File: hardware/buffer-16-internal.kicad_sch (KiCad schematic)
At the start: 6 parts, among them U2 SN74LVC8T245DWRG4, U3 SN74LVC8T245DWRG4

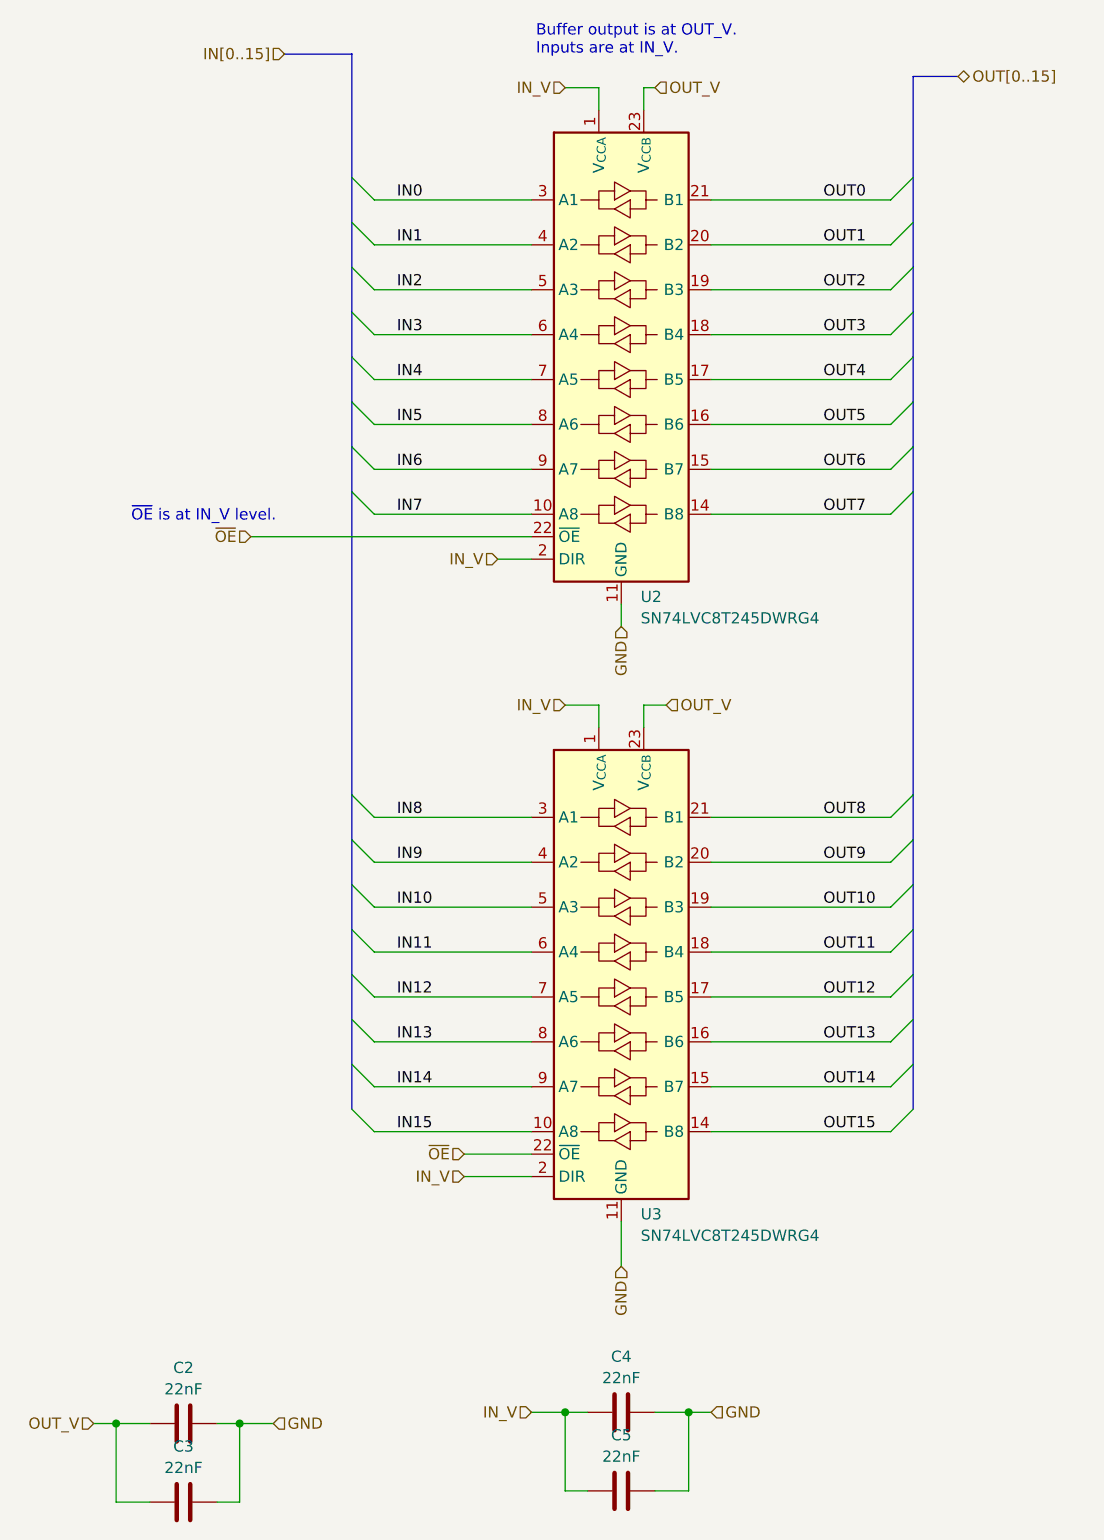
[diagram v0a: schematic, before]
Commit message: Massively reorganize board designs
Now planning to have most assembly done by JLCPCB, so trace sizes,
part selections, etc. are set accordingly.

New boards are:
 - cartridge interface & flash
 - microcontroller & registers
 - sram x2
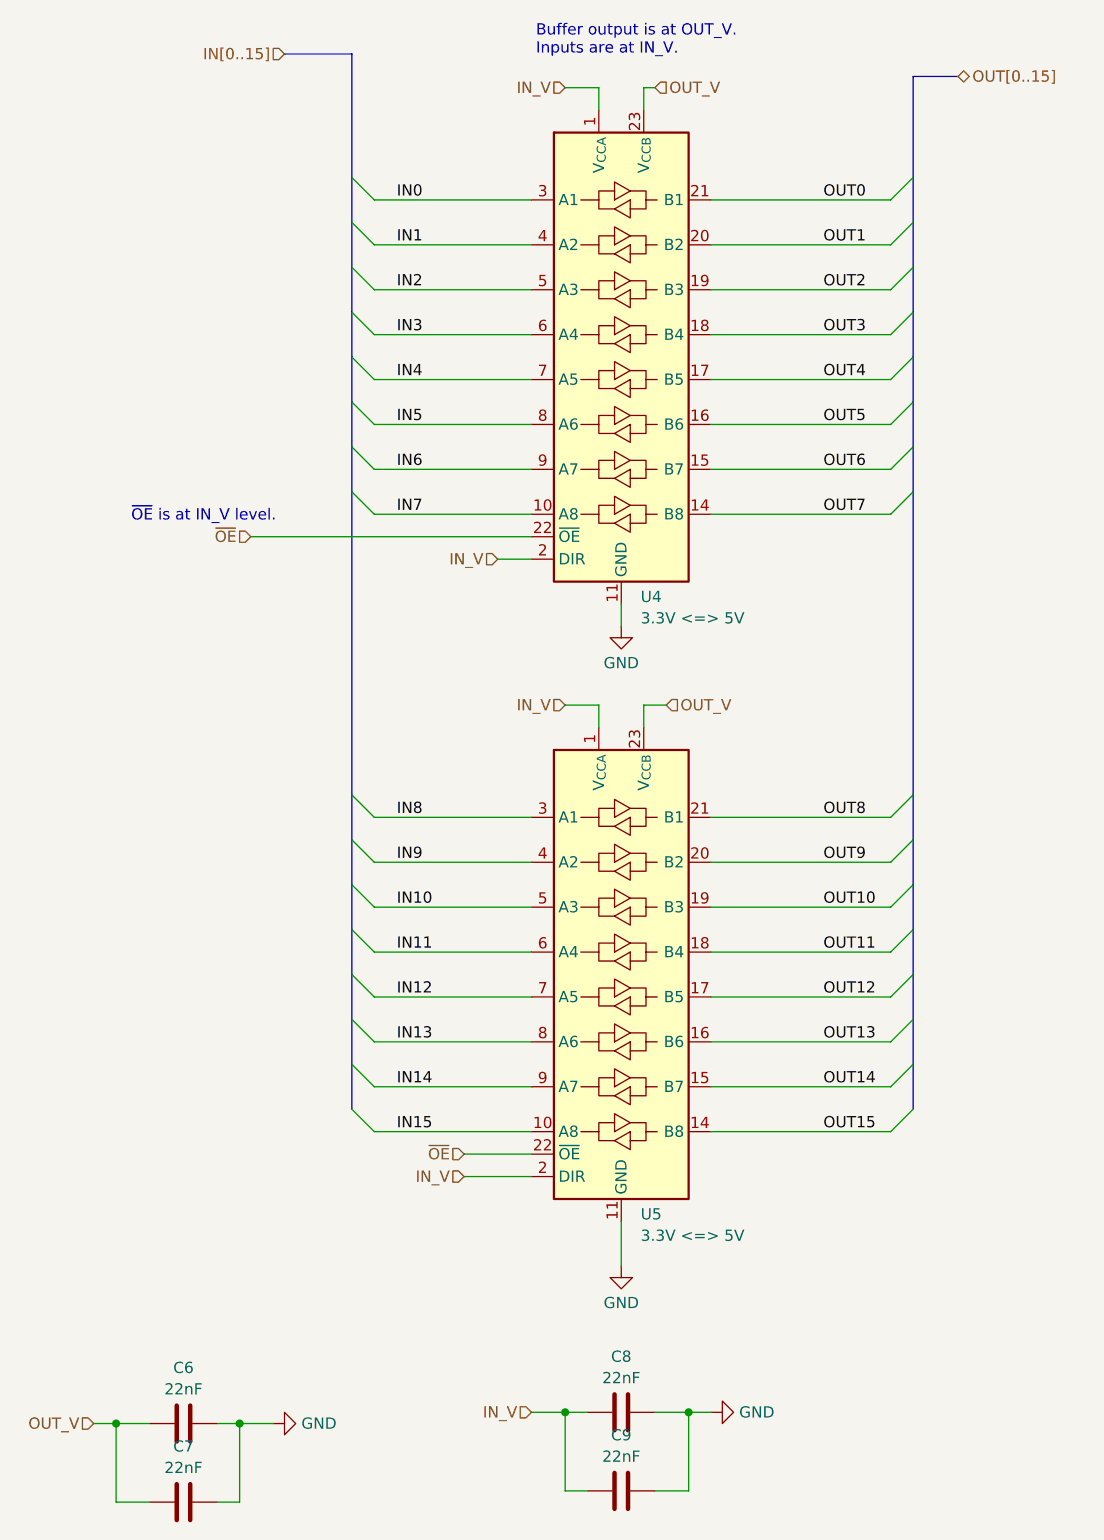
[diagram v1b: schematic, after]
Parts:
- C6: renamed from C2; footprint Capacitor_SMD:C_1206_3216Metric -> Capacitor_SMD:C_0603_1608Metric; JLCPCB Part Number (none) -> CL10B223KB8NNNC; Mouser Part Number (none) -> 80-C0603C223K4R; Part Number (none) -> C0603C223K4RACTU
- C7: renamed from C3; footprint Capacitor_SMD:C_1206_3216Metric -> Capacitor_SMD:C_0603_1608Metric; JLCPCB Part Number (none) -> CL10B223KB8NNNC; Mouser Part Number (none) -> 80-C0603C223K4R; Part Number (none) -> C0603C223K4RACTU
- C8: renamed from C4; footprint Capacitor_SMD:C_1206_3216Metric -> Capacitor_SMD:C_0603_1608Metric; JLCPCB Part Number (none) -> CL10B223KB8NNNC; Mouser Part Number (none) -> 80-C0603C223K4R; Part Number (none) -> C0603C223K4RACTU
- C9: renamed from C5; footprint Capacitor_SMD:C_1206_3216Metric -> Capacitor_SMD:C_0603_1608Metric; JLCPCB Part Number (none) -> CL10B223KB8NNNC; Mouser Part Number (none) -> 80-C0603C223K4R; Part Number (none) -> C0603C223K4RACTU
- U4: renamed from U2; value SN74LVC8T245DWRG4 -> 3.3V <=> 5V; footprint Package_SO:SOIC-24W_7.5x15.4mm_P1.27mm -> Package_SO:SSOP-24_5.3x8.2mm_P0.65mm; JLCPCB Part Number (none) -> C19197; Mouser Part Number (none) -> 595-SN74LVC8T245DBR; Part Number (none) -> SN74LVC8T245DBR
- U5: renamed from U3; value SN74LVC8T245DWRG4 -> 3.3V <=> 5V; footprint Package_SO:SOIC-24W_7.5x15.4mm_P1.27mm -> Package_SO:SSOP-24_5.3x8.2mm_P0.65mm; JLCPCB Part Number (none) -> C19197; Mouser Part Number (none) -> 595-SN74LVC8T245DBR; Part Number (none) -> SN74LVC8T245DBR

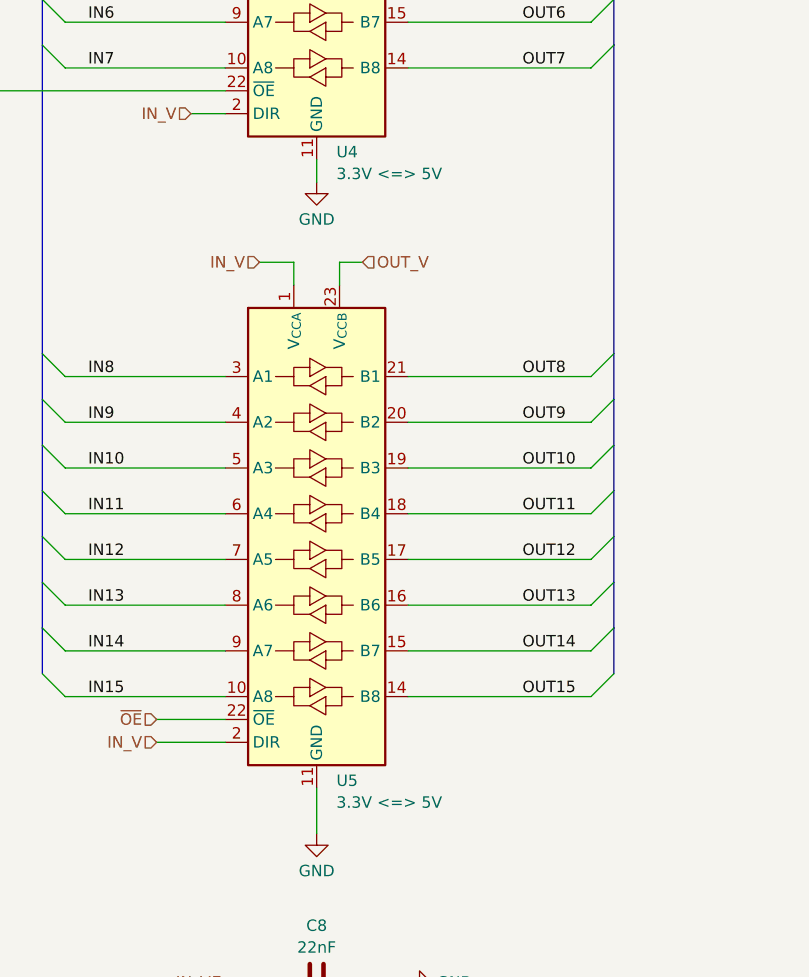
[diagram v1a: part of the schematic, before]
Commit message: Redesign SRAM address decoders
 - Redo original address decoder for SRAM_CE signal
 - Replace NAND gate with another address decoder
   - Simplifies the BOM by removing a one-off part
   - Stabilizes the control signals by making sure SEGA_CONTROL and
     UC_CONTROL can never be active at once (one does not depend on
     the other)
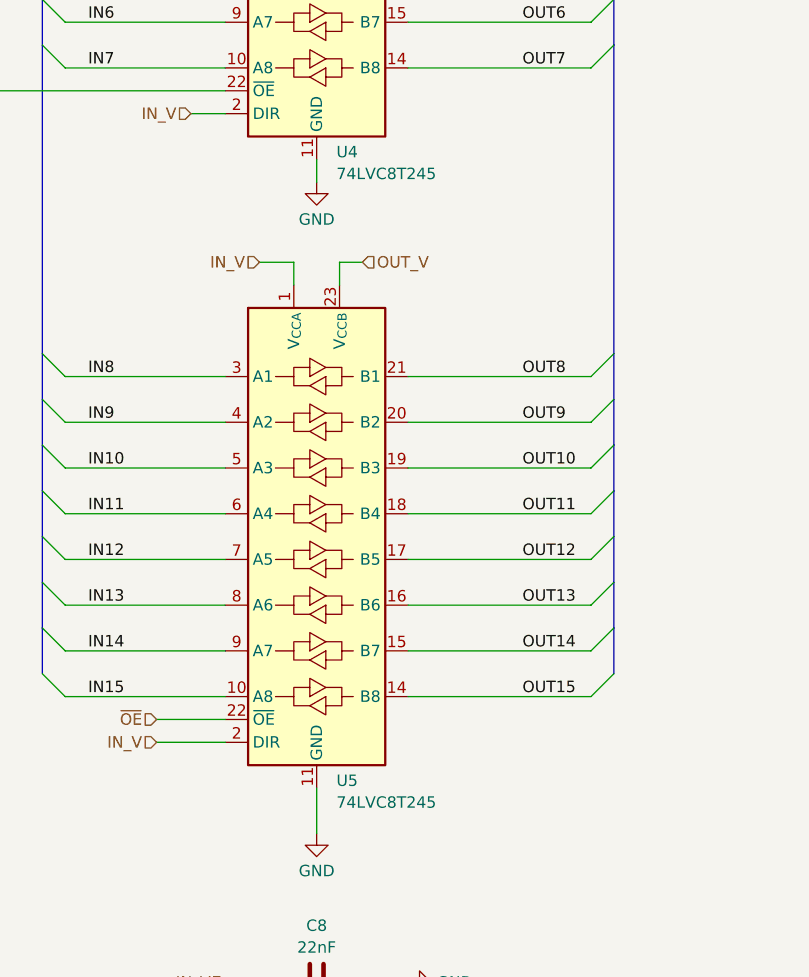
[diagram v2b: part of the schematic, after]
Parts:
- U4, U5: value 3.3V <=> 5V -> 74LVC8T245
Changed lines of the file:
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@@
 			)
 		)
-		(property "Value" "3.3V <=> 5V"
+		(property "Value" "74LVC8T245"
 			(at 129.1941 86.6944 0)
 			(effects
@@
 			)
 		)
-		(property "Value" "3.3V <=> 5V"
+		(property "Value" "74LVC8T245"
 			(at 129.1941 156.5444 0)
 			(effects

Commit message: Replace 8-bit buffers with cheaper version
Replace SN74LVC8T245DBR (8-bit buffers) with SN74LVC8T245PWR.  The old
version was SSOP, and the new version is a TSSOP size, but they are
otherwise the same.

This is estimated to reduce the price of a complete unit by over $11,
or about 16.5%.
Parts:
- U4, U5: footprint Package_SO:SSOP-24_5.3x8.2mm_P0.65mm -> Package_SO:TSSOP-24_4.4x7.8mm_P0.65mm; JLCPCB Part Number C19197 -> C27643; Mouser Part Number 595-SN74LVC8T245DBR -> 595-SN74LVC8T245PWR; Part Number SN74LVC8T245DBR -> SN74LVC8T245PWR
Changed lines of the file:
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@@
 			)
 		)
-		(property "Footprint" "Package_SO:SSOP-24_5.3x8.2mm_P0.65mm"
+		(property "Footprint" "Package_SO:TSSOP-24_4.4x7.8mm_P0.65mm"
 			(at 147.32 81.28 0)
 			(effects
@@
 			)
 		)
-		(property "Datasheet" "https://www.ti.com/lit/ds/symlink/sn74lvc8t245.pdf"
+		(property "Datasheet" "https://www.ti.com/lit/gpn/sn74lvc8t245"
 			(at 127 92.71 0)
 			(effects
@@
 			)
 		)
-		(property "JLCPCB Part Number" "C19197"
+		(property "JLCPCB Part Number" "C27643"
 			(at 127 57.15 0)
 			(effects
@@
 			)
 		)
-		(property "Mouser Part Number" "595-SN74LVC8T245DBR"
+		(property "Mouser Part Number" "595-SN74LVC8T245PWR"
 			(at 127 57.15 0)
 			(effects
@@
 			)
 		)
-		(property "Part Number" "SN74LVC8T245DBR"
+		(property "Part Number" "SN74LVC8T245PWR"
 			(at 127 57.15 0)
 			(effects
@@
 			)
 		)
-		(property "Footprint" "Package_SO:SSOP-24_5.3x8.2mm_P0.65mm"
+		(property "Footprint" "Package_SO:TSSOP-24_4.4x7.8mm_P0.65mm"
 			(at 147.32 151.13 0)
 			(effects
@@
 			)
 		)
-		(property "Datasheet" "https://www.ti.com/lit/ds/symlink/sn74lvc8t245.pdf"
+		(property "Datasheet" "https://www.ti.com/lit/gpn/sn74lvc8t245"
 			(at 127 162.56 0)
 			(effects
@@
 			)
 		)
-		(property "JLCPCB Part Number" "C19197"
+		(property "JLCPCB Part Number" "C27643"
 			(at 127 127 0)
 			(effects
@@
 			)
 		)
-		(property "Mouser Part Number" "595-SN74LVC8T245DBR"
+		(property "Mouser Part Number" "595-SN74LVC8T245PWR"
 			(at 127 127 0)
 			(effects
@@
 			)
 		)
-		(property "Part Number" "SN74LVC8T245DBR"
+		(property "Part Number" "SN74LVC8T245PWR"
 			(at 127 127 0)
 			(effects
